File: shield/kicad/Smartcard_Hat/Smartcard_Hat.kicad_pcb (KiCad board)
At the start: 2 copper layers, 68.6 x 53.3 mm, 11 parts, among them J1 7712P0225A25LF, U6 ST8034HNQR

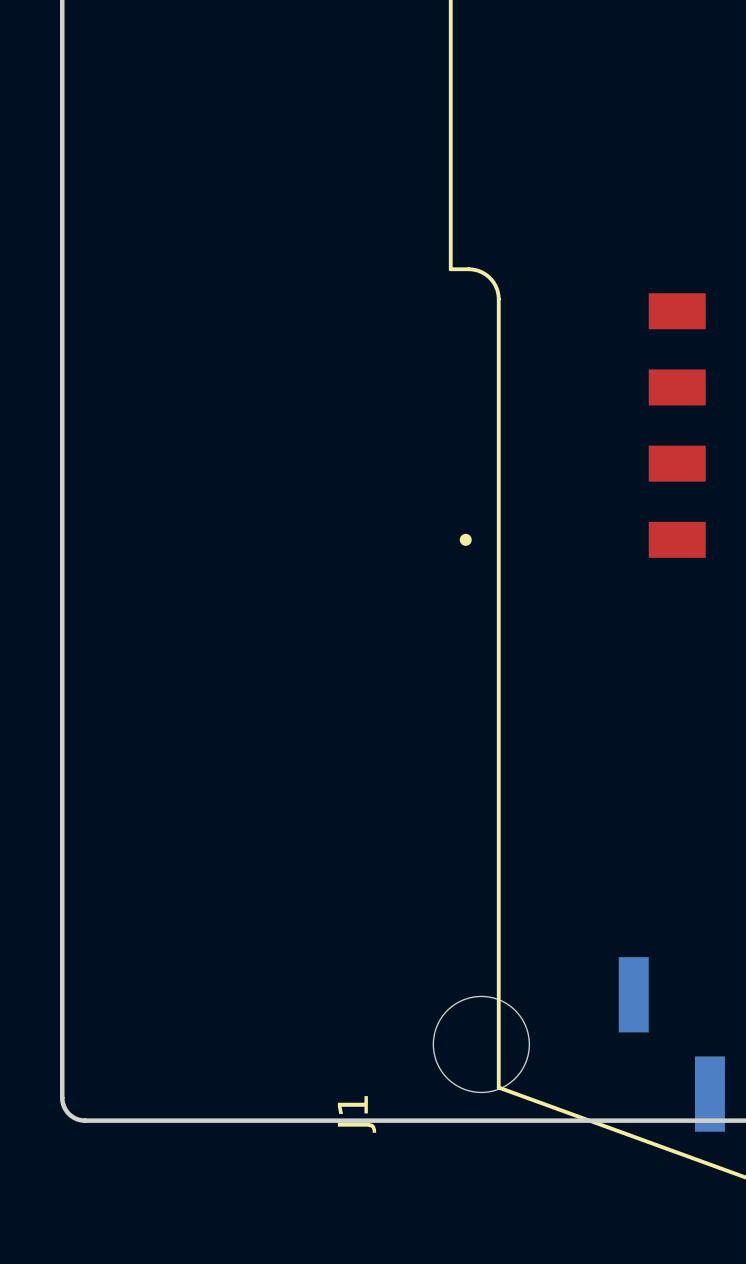
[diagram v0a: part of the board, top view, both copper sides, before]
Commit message: add basic qr scanner
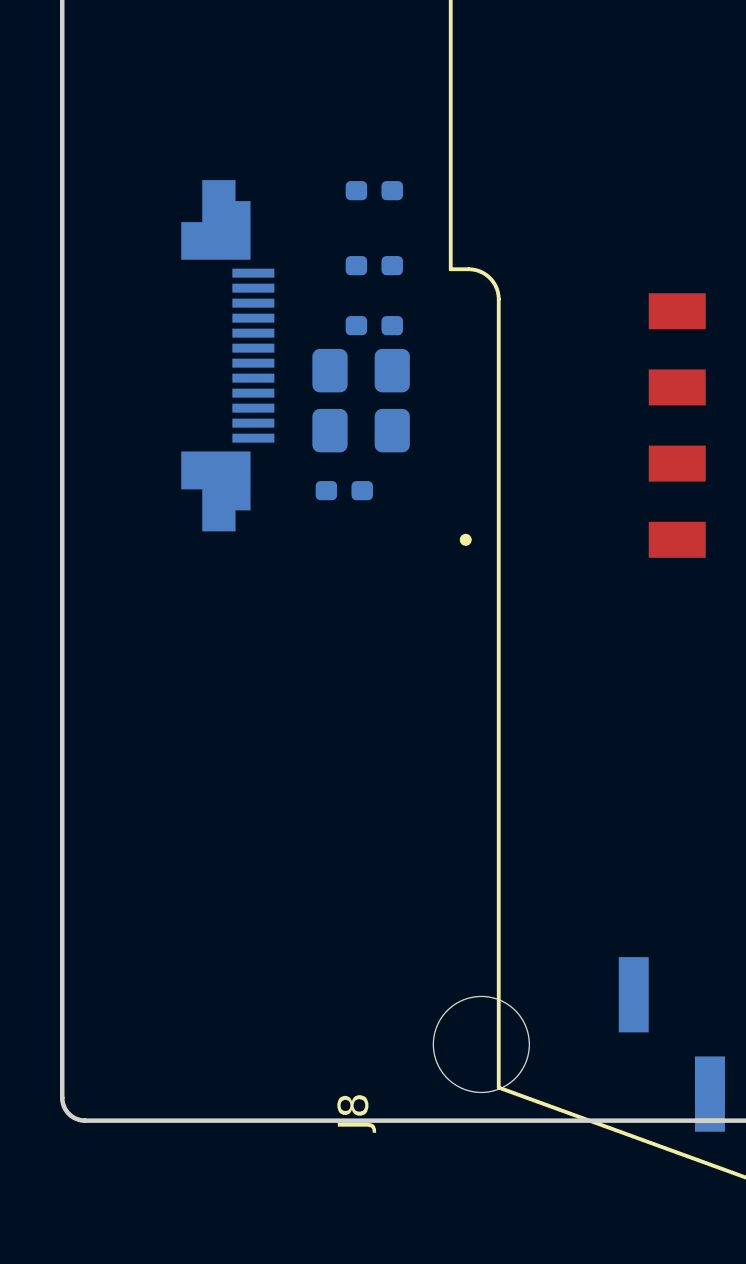
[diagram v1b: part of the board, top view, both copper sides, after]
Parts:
- added C41: 1u, Capacitor_SMD:C_0805_2012Metric_Pad1.18x1.45mm_HandSolder, B.Cu at (110.0, 75.0)
- added C42: 22u, Capacitor_SMD:C_0805_2012Metric_Pad1.18x1.45mm_HandSolder, B.Cu at (110.0, 77.0)
- added J10: SFV12R-2STE1HLF, Library:AMPHENOL_SFV12R-2STE1HLF, B.Cu at (104.0, 74.5)
- added R48: 10k, Resistor_SMD:R_0402_1005Metric_Pad0.72x0.64mm_HandSolder, B.Cu at (110.4, 69.0)
- added R49: 10k, Resistor_SMD:R_0402_1005Metric_Pad0.72x0.64mm_HandSolder, B.Cu at (110.4, 71.5)
- added R50: 10k, Resistor_SMD:R_0402_1005Metric_Pad0.72x0.64mm_HandSolder, B.Cu at (109.4, 79.0)
- added R51: 200R, Resistor_SMD:R_0402_1005Metric_Pad0.72x0.64mm_HandSolder, B.Cu at (110.4, 73.5)
- renumbered J1 to J8
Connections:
- J12 pad 1: /7 -> /QR_UART_TX
- J12 pad 2: /*6 -> /QR_UART_RX
- J12 pad 3: /*5 -> unconnected-(J12-Pin_3-Pad3)
- J12 pad 4: /4 -> unconnected-(J12-Pin_4-Pad4)
- J12 pad 5: /*3 -> unconnected-(J12-Pin_5-Pad5)
- J12 pad 6: /2 -> unconnected-(J12-Pin_6-Pad6)
- J12 pad 7: /TX/1 -> unconnected-(J12-Pin_7-Pad7)
- J12 pad 8: /RX/0 -> unconnected-(J12-Pin_8-Pad8)
- J8 pad C1: Net-(J1-VCC) -> Net-(J8-VCC)
- J8 pad C2: Net-(J1-RST) -> Net-(J8-RST)
- J8 pad C3: Net-(J1-CLK) -> Net-(J8-CLK)
- J8 pad C4: Net-(J1-RFU) -> Net-(J8-RFU)
- J8 pad C7: Net-(J1-I/O) -> Net-(J8-I/O)
- J8 pad C8: Net-(J1-RFU__1) -> Net-(J8-RFU__1)

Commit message: re-org
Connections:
- net /NRST renamed /STM32F469I-DISCO-Interface/NRST
- net /QR_BEEP renamed /QR_Scanner/QR_BEEP
- J10 pad 10: /QR_TRIG -> unconnected-(J10-Pad10)
- J10 pad 12: unconnected-(J10-Pad12) -> /QR_Scanner/QR_TRIG
- J10 pad 5: /QR_UART_TX -> /QR_Scanner/QR_UART_TX
- J11 pad 1: /SCL/A5 -> unconnected-(J11-Pin_1-Pad1)
- J11 pad 10: /8 -> unconnected-(J11-Pin_10-Pad10)
- J11 pad 2: /SDA/A4 -> unconnected-(J11-Pin_2-Pad2)
- J11 pad 3: /AREF -> unconnected-(J11-Pin_3-Pad3)
- J11 pad 5: /13 -> unconnected-(J11-Pin_5-Pad5)
- J11 pad 6: /12 -> unconnected-(J11-Pin_6-Pad6)
- J11 pad 7: /*11 -> unconnected-(J11-Pin_7-Pad7)
- J11 pad 8: /*10 -> unconnected-(J11-Pin_8-Pad8)
- J11 pad 9: /*9 -> unconnected-(J11-Pin_9-Pad9)
- J12 pad 1: /QR_UART_TX -> /STM32F469I-DISCO-Interface/QR_UART_TX
- J12 pad 2: /QR_UART_RX -> /STM32F469I-DISCO-Interface/QR_UART_RX
- J13 pad 1: /A0 -> unconnected-(J13-Pin_1-Pad1)
- J13 pad 2: /A1 -> unconnected-(J13-Pin_2-Pad2)
- J13 pad 3: /A2 -> unconnected-(J13-Pin_3-Pad3)
- J13 pad 4: /A3 -> unconnected-(J13-Pin_4-Pad4)
- J13 pad 5: /SDA/A4 -> unconnected-(J13-Pin_5-Pad5)
- J13 pad 6: /SCL/A5 -> unconnected-(J13-Pin_6-Pad6)
- J8 pad NO: Net-(U6-*PRES) -> Net-(U1-*PRES)
- R48 pad 2: /QR_TRIG -> /QR_Scanner/QR_TRIG
- R49 pad 2: /QR_UART_TX -> /QR_Scanner/QR_UART_TX
- R51 pad 1: /QR_UART_RX -> /QR_Scanner/QR_UART_RX
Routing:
- net (no net): track 0.00 -> 2.35 mm
- net /SDA/A4: track 1.18 -> 0.00 mm
- net /SCL/A5: track 1.18 -> 0.00 mm

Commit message: wip
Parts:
- added C28: u1, Capacitor_SMD:C_0805_2012Metric_Pad1.18x1.45mm_HandSolder, F.Cu at (151.1, 71.0)
- added C29: u1, Capacitor_SMD:C_0805_2012Metric_Pad1.18x1.45mm_HandSolder, F.Cu at (151.1, 74.0)
- added C30: u1, Capacitor_SMD:C_0805_2012Metric_Pad1.18x1.45mm_HandSolder, F.Cu at (151.1, 77.1)
- added C31: u1, Capacitor_SMD:C_0805_2012Metric_Pad1.18x1.45mm_HandSolder, F.Cu at (151.1, 80.1)
- added C32: u1, Capacitor_SMD:C_0805_2012Metric_Pad1.18x1.45mm_HandSolder, F.Cu at (151.1, 83.1)
- added C33: u1, Capacitor_SMD:C_0805_2012Metric_Pad1.18x1.45mm_HandSolder, F.Cu at (155.9, 71.0)
- added C34: u1, Capacitor_SMD:C_0805_2012Metric_Pad1.18x1.45mm_HandSolder, F.Cu at (155.9, 74.0)
- added C35: 22u, Capacitor_SMD:C_0805_2012Metric_Pad1.18x1.45mm_HandSolder, F.Cu at (155.9, 77.1)
- added C36: u1, Capacitor_SMD:C_0805_2012Metric_Pad1.18x1.45mm_HandSolder, F.Cu at (155.9, 80.1)
- added C39: 1n, Capacitor_SMD:C_0805_2012Metric_Pad1.18x1.45mm_HandSolder, F.Cu at (155.9, 83.1)
- added R31: 24k, Resistor_SMD:R_0402_1005Metric_Pad0.72x0.64mm_HandSolder, F.Cu at (159.9, 70.5)
- added R32: 10k, Resistor_SMD:R_0402_1005Metric_Pad0.72x0.64mm_HandSolder, F.Cu at (159.9, 72.5)
- added R33: 10k, Resistor_SMD:R_0402_1005Metric_Pad0.72x0.64mm_HandSolder, F.Cu at (159.9, 74.5)
- added R34: 10k, Resistor_SMD:R_0402_1005Metric_Pad0.72x0.64mm_HandSolder, F.Cu at (159.9, 76.5)
- added R35: 10k, Resistor_SMD:R_0402_1005Metric_Pad0.72x0.64mm_HandSolder, F.Cu at (159.9, 78.5)
- added R36: 200R, Resistor_SMD:R_0402_1005Metric_Pad0.72x0.64mm_HandSolder, F.Cu at (163.2, 70.5)
- added R40: 200R, Resistor_SMD:R_0402_1005Metric_Pad0.72x0.64mm_HandSolder, F.Cu at (163.2, 72.5)
- added R41: 200R, Resistor_SMD:R_0402_1005Metric_Pad0.72x0.64mm_HandSolder, F.Cu at (163.2, 74.5)
- added R42: 200R, Resistor_SMD:R_0402_1005Metric_Pad0.72x0.64mm_HandSolder, F.Cu at (163.2, 76.5)
- added R43: 10k, Resistor_SMD:R_0402_1005Metric_Pad0.72x0.64mm_HandSolder, F.Cu at (163.2, 78.5)
- added R44: 200R, Resistor_SMD:R_0402_1005Metric_Pad0.72x0.64mm_HandSolder, F.Cu at (166.4, 70.5)
- added R45: 11.3k, Resistor_SMD:R_0402_1005Metric_Pad0.72x0.64mm_HandSolder, F.Cu at (166.4, 72.5)
- added R46: 10k, Resistor_SMD:R_0402_1005Metric_Pad0.72x0.64mm_HandSolder, F.Cu at (166.4, 74.5)
- added R47: 10k, Resistor_SMD:R_0402_1005Metric_Pad0.72x0.64mm_HandSolder, F.Cu at (166.4, 76.5)
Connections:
- J11 pad 1: unconnected-(J11-Pin_1-Pad1) -> /STM32F469I-DISCO-Interface/SC_RST
- J11 pad 2: unconnected-(J11-Pin_2-Pad2) -> /STM32F469I-DISCO-Interface/SC_AUX2
- J11 pad 4: GND -> unconnected-(J11-Pin_4-Pad4)
- J11 pad 7: unconnected-(J11-Pin_7-Pad7) -> GND
- J12 pad 3: unconnected-(J12-Pin_3-Pad3) -> /STM32F469I-DISCO-Interface/QR_TRIG
- J12 pad 4: unconnected-(J12-Pin_4-Pad4) -> /STM32F469I-DISCO-Interface/UC_BEEP
- J12 pad 5: unconnected-(J12-Pin_5-Pad5) -> /STM32F469I-DISCO-Interface/SC_CLKDIV2
- J12 pad 6: unconnected-(J12-Pin_6-Pad6) -> /STM32F469I-DISCO-Interface/SC_IO
- J12 pad 7: unconnected-(J12-Pin_7-Pad7) -> /STM32F469I-DISCO-Interface/SC_AUX1
- J12 pad 8: unconnected-(J12-Pin_8-Pad8) -> /STM32F469I-DISCO-Interface/SC_CLKDIV1
- J13 pad 2: unconnected-(J13-Pin_2-Pad2) -> /STM32F469I-DISCO-Interface/SC_nOFF
- J13 pad 3: unconnected-(J13-Pin_3-Pad3) -> /STM32F469I-DISCO-Interface/SC_VCC_SEL1
- J13 pad 4: unconnected-(J13-Pin_4-Pad4) -> /STM32F469I-DISCO-Interface/SC_VCC_SEL2
- J13 pad 5: unconnected-(J13-Pin_5-Pad5) -> /STM32F469I-DISCO-Interface/SC_nCMDVCC
- J13 pad 6: unconnected-(J13-Pin_6-Pad6) -> /STM32F469I-DISCO-Interface/SC_CLK

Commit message: wip
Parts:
- added R52: 10k, Resistor_SMD:R_0402_1005Metric_Pad0.72x0.64mm_HandSolder, B.Cu at (155.9, 62.0)
- C28, C29, C30, C31, C32, C33, C34, C35, C36, C39, R31, R32, R33, R34, R35, R36, R40, R41, R42, R43, R45, R46, R47: moved to B.Cu
- R44: value 200R -> 22R; moved to B.Cu
- moved R43 35.1 mm to (128.6, 84.5)
- moved R41 31.1 mm to (132.1, 73.0), turned to 180 degrees
- moved R42 26.6 mm to (136.6, 75.0)
- moved U6 20.5 mm to (134.4, 86.8)
- moved R35 20.4 mm to (141.6, 87.5), turned to 180 degrees
- moved R36 12.8 mm to (150.4, 70.5), turned to 180 degrees
- moved R40 12.8 mm to (150.4, 72.5), turned to 180 degrees
- moved C28 11.4 mm to (162.5, 71.0), turned to 180 degrees
- moved C29 11.4 mm to (162.5, 74.0), turned to 180 degrees
- moved C30 11.4 mm to (162.5, 77.1), turned to 180 degrees
- moved C31 11.4 mm to (162.5, 80.1), turned to 180 degrees
- moved C32 11.4 mm to (162.5, 83.1), turned to 180 degrees
- moved R31 6.29 mm to (153.6, 70.5), turned to 180 degrees
- moved R32 6.29 mm to (153.6, 72.5), turned to 180 degrees
- moved R33 6.29 mm to (153.6, 74.5), turned to 180 degrees
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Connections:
- C30 pad 1: GND -> Net-(J8-VCC)
- C30 pad 2: Net-(J8-VCC) -> GND
- C31 pad 1: GND -> Net-(J8-VCC)
- C31 pad 2: Net-(J8-VCC) -> GND
- C39 pad 1: Net-(U1-PORADJ) -> Net-(U6-PORADJ)
- J8 pad NO: Net-(U1-*PRES) -> Net-(U6-*PRES)
- R31 pad 2: Net-(U1-*OFF) -> /SmartCard_Reader/SC_nOFF
- R35 pad 2: /SmartCard_Reader/SC_nCMDVCC -> Net-(U6-*CMDVCC)
- R36 pad 1: Net-(U1-*OFF) -> /SmartCard_Reader/SC_nCMDVCC
- R36 pad 2: /SmartCard_Reader/SC_nOFF -> Net-(U6-*CMDVCC)
- R40 pad 2: Net-(U1-I/OUC) -> Net-(U6-I/OUC)
- R41 pad 2: Net-(U1-AUXUC1) -> Net-(U6-AUXUC1)
- R42 pad 2: Net-(U1-AUXUC2) -> Net-(U6-AUXUC2)
- R43 pad 2: Net-(U1-PORADJ) -> Net-(U6-PORADJ)
- R44 pad 2: Net-(U1-XTAL1) -> Net-(U6-XTAL1)
- R45 pad 1: Net-(U1-PORADJ) -> Net-(U6-PORADJ)
- U6 pad 1: unconnected-(U6-VDD(INTF)-Pad1) -> +3V3
- U6 pad 10: Net-(J1-RFU) -> Net-(J8-RFU)
- U6 pad 11: Net-(J1-RFU__1) -> Net-(J8-RFU__1)
- U6 pad 13: Net-(J1-CLK) -> Net-(J8-CLK)
- U6 pad 14: Net-(J1-RST) -> Net-(J8-RST)
- U6 pad 15: Net-(J1-VCC) -> Net-(J8-VCC)
- U6 pad 18: unconnected-(U6-PORADJ-Pad18) -> Net-(U6-PORADJ)
- U6 pad 19: unconnected-(U6-*OFF-Pad19) -> /SmartCard_Reader/SC_nOFF
- U6 pad 2: unconnected-(U6-VCC_SEL2-Pad2) -> /SmartCard_Reader/SC_VCC_SEL2
- U6 pad 20: unconnected-(U6-I/OUC-Pad20) -> Net-(U6-I/OUC)
- U6 pad 21: unconnected-(U6-AUXUC1-Pad21) -> Net-(U6-AUXUC1)
- U6 pad 22: unconnected-(U6-AUXUC2-Pad22) -> Net-(U6-AUXUC2)
- U6 pad 23: unconnected-(U6-XTAL1-Pad23) -> Net-(U6-XTAL1)
- U6 pad 3: unconnected-(U6-RSTIN-Pad3) -> /SmartCard_Reader/SC_RST
- U6 pad 4: unconnected-(U6-VCC_SEL1-Pad4) -> /SmartCard_Reader/SC_VCC_SEL1
- U6 pad 5: unconnected-(U6-*CMDVCC-Pad5) -> Net-(U6-*CMDVCC)
- U6 pad 6: unconnected-(U6-CLKDIV1-Pad6) -> /SmartCard_Reader/SC_CLKDIV1
- U6 pad 7: unconnected-(U6-CLKDIV2-Pad7) -> /SmartCard_Reader/SC_CLKDIV2
- U6 pad 9: Net-(J1-I/O) -> Net-(J8-I/O)

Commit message: wip
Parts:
- removed MH1, MH2, MH3, MH4: MountingHole_3.2mm, Arduino_MountingHole:MountingHole_3.2mm
- C28, C29, C30, C31, C32, C33, C34, C39, C41, C42, J10, R31, R36, R40, R41, R42, R43, R44, R45, R48, R49, R50, R51, R52: moved to F.Cu
- J11: footprint Connector_PinHeader_2.54mm:PinHeader_1x10_P2.54mm_Vertical_SMD_Pin1Left -> Connector_PinHeader_2.54mm:PinHeader_1x10_P2.54mm_Vertical_SMD_Pin1Right
- J12, J9: footprint Connector_PinHeader_2.54mm:PinHeader_1x08_P2.54mm_Vertical_SMD_Pin1Left -> Connector_PinHeader_2.54mm:PinHeader_1x08_P2.54mm_Vertical_SMD_Pin1Right
- J13: footprint Connector_PinHeader_2.54mm:PinHeader_1x06_P2.54mm_Vertical_SMD_Pin1Left -> Connector_PinHeader_2.54mm:PinHeader_1x06_P2.54mm_Vertical_SMD_Pin1Right
- J8: footprint 7312P0225A13LF:AMPHENOL_7312P0225A13LF -> Library:AMPHENOL_7312P0225A13LF
- U6: footprint footprints:QFN24_4x4x0.8_STM -> Library:QFN24_4x4x0.8_STM; moved to F.Cu
- moved J11 61.7 mm to (177.2, 69.0), turned to 0 degrees
- moved R43 58.1 mm to (178.0, 53.9), turned to 90 degrees
- moved R44 56.8 mm to (128.7, 113.0), turned to 0 degrees
- moved J12 56.4 mm to (177.2, 96.0), turned to 0 degrees
- moved U6 53.4 mm to (167.5, 44.8), turned to -90 degrees
- moved R41 53.2 mm to (176.8, 44.1)
- moved C41 53.2 mm to (160.5, 58.2), turned to -90 degrees
- moved R42 51.8 mm to (176.8, 42.5), turned to 180 degrees
- moved C42 51.6 mm to (158.0, 58.2), turned to -90 degrees
- moved J10 49.6 mm to (150.3, 56.9), turned to 180 degrees
- moved R35 49.4 mm to (163.5, 43.2), turned to -90 degrees
- moved R46 41.4 mm to (163.0, 33.2), turned to 90 degrees
- moved R32 41.2 mm to (166.0, 33.2), turned to 90 degrees
- moved R50 39.4 mm to (142.2, 57.2), turned to 0 degrees
- moved R47 38.6 mm to (168.8, 38.0), turned to -90 degrees
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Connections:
- J10 pad 12: /QR_Scanner/QR_TRIG -> QR_TRIG
- J10 pad 5: /QR_Scanner/QR_UART_TX -> QR_UART_TX
- J10 pad 9: /QR_Scanner/QR_BEEP -> UC_BEEP
- J11 pad 1: /STM32F469I-DISCO-Interface/SC_RST -> SC_RST
- J11 pad 2: /STM32F469I-DISCO-Interface/SC_AUX2 -> SC_AUX2
- J12 pad 1: /STM32F469I-DISCO-Interface/QR_UART_TX -> QR_UART_TX
- J12 pad 2: /STM32F469I-DISCO-Interface/QR_UART_RX -> QR_UART_RX
- J12 pad 3: /STM32F469I-DISCO-Interface/QR_TRIG -> QR_TRIG
- J12 pad 4: /STM32F469I-DISCO-Interface/UC_BEEP -> UC_BEEP
- J12 pad 5: /STM32F469I-DISCO-Interface/SC_CLKDIV2 -> SC_CLKDIV2
- J12 pad 6: /STM32F469I-DISCO-Interface/SC_IO -> SC_IO
- J12 pad 7: /STM32F469I-DISCO-Interface/SC_AUX1 -> SC_AUX1
- J12 pad 8: /STM32F469I-DISCO-Interface/SC_CLKDIV1 -> SC_CLKDIV1
- J13 pad 2: /STM32F469I-DISCO-Interface/SC_nOFF -> SC_nOFF
- J13 pad 3: /STM32F469I-DISCO-Interface/SC_VCC_SEL1 -> SC_VCC_SEL1
- J13 pad 4: /STM32F469I-DISCO-Interface/SC_VCC_SEL2 -> SC_VCC_SEL2
- J13 pad 5: /STM32F469I-DISCO-Interface/SC_nCMDVCC -> SC_nCMDVCC
- J13 pad 6: /STM32F469I-DISCO-Interface/SC_CLK -> SC_CLK
- R31 pad 2: /SmartCard_Reader/SC_nOFF -> Net-(U6-*OFF)
- R32 pad 2: /SmartCard_Reader/SC_CLKDIV1 -> SC_CLKDIV1
- R33 pad 2: /SmartCard_Reader/SC_VCC_SEL2 -> SC_VCC_SEL2
- R34 pad 2: /SmartCard_Reader/SC_VCC_SEL1 -> SC_VCC_SEL1
- R35 pad 2: Net-(U6-*CMDVCC) -> SC_nCMDVCC
- R36 pad 1: /SmartCard_Reader/SC_nCMDVCC -> SC_nOFF
- R36 pad 2: Net-(U6-*CMDVCC) -> Net-(U6-*OFF)
- R40 pad 1: /SmartCard_Reader/SC_IO -> SC_IO
- R41 pad 1: /SmartCard_Reader/SC_AUX1 -> SC_AUX1
- R42 pad 1: /SmartCard_Reader/SC_AUX2 -> SC_AUX2
- R44 pad 1: /SmartCard_Reader/SC_CLK -> SC_CLK
- R46 pad 1: /SmartCard_Reader/SC_CLKDIV2 -> SC_CLKDIV2
- R47 pad 1: /SmartCard_Reader/SC_RST -> SC_RST
- R48 pad 2: /QR_Scanner/QR_TRIG -> QR_TRIG
- R49 pad 2: /QR_Scanner/QR_UART_TX -> QR_UART_TX
- R51 pad 1: /QR_Scanner/QR_UART_RX -> QR_UART_RX
- U6 pad 19: /SmartCard_Reader/SC_nOFF -> Net-(U6-*OFF)
- U6 pad 2: /SmartCard_Reader/SC_VCC_SEL2 -> SC_VCC_SEL2
- U6 pad 3: /SmartCard_Reader/SC_RST -> SC_RST
- U6 pad 4: /SmartCard_Reader/SC_VCC_SEL1 -> SC_VCC_SEL1
- U6 pad 5: Net-(U6-*CMDVCC) -> SC_nCMDVCC
- U6 pad 6: /SmartCard_Reader/SC_CLKDIV1 -> SC_CLKDIV1
- U6 pad 7: /SmartCard_Reader/SC_CLKDIV2 -> SC_CLKDIV2
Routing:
- net +3V3: track 0.00 -> 71.4 mm, vias 0 -> 1
- net GND: track 1.18 -> 31.2 mm, vias 0 -> 1
- net Net-(J10-Pad4): track 0.00 -> 13.0 mm
- net QR_UART_TX: track 0.00 -> 11.6 mm
- net Net-(U6-*OFF): track 0.00 -> 9.15 mm
- net Net-(U6-XTAL1): track 0.00 -> 8.15 mm
- net Net-(U6-AUXUC2): track 0.00 -> 7.66 mm
- net Net-(U6-AUXUC1): track 0.00 -> 7.16 mm
- net Net-(U6-I/OUC): track 0.00 -> 6.95 mm
- net QR_TRIG: track 0.00 -> 4.89 mm
- net (no net): track 2.35 -> 0.00 mm
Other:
- board size 68.6 x 53.3 mm -> 60 x 127 mm

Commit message: wip
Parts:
- added R1000: 0R, Resistor_SMD:R_0805_2012Metric_Pad1.20x1.40mm_HandSolder, F.Cu at (161.2, 46.8)
- added R1001: 0R, Resistor_SMD:R_0805_2012Metric_Pad1.20x1.40mm_HandSolder, F.Cu at (167.5, 38.0)
- C35, C36: moved to F.Cu
- J8: footprint Library:AMPHENOL_7312P0225A13LF -> 7312P0225A13LF:AMPHENOL_7312P0225A13LF
- R31, R36, R40, R41, R42, R43, R45, R48, R49, R50, R51, R52: footprint Resistor_SMD:R_0402_1005Metric_Pad0.72x0.64mm_HandSolder -> Resistor_SMD:R_0805_2012Metric_Pad1.20x1.40mm_HandSolder
- R32, R33, R34, R35, R46, R47: footprint Resistor_SMD:R_0402_1005Metric_Pad0.72x0.64mm_HandSolder -> Resistor_SMD:R_0805_2012Metric_Pad1.20x1.40mm_HandSolder; moved to F.Cu
- R44: footprint Resistor_SMD:R_0402_1005Metric_Pad0.72x0.64mm_HandSolder -> Resistor_SMD:R_0805_2012Metric_Pad1.20x1.40mm_HandSolder; moved to B.Cu
- moved R46 9.51 mm to (162.5, 42.8), turned to 180 degrees
- moved R32 8.96 mm to (158.4, 38.0), turned to -90 degrees
- moved R33 8.36 mm to (165.2, 38.0)
- moved R35 5.96 mm to (160.7, 38.0)
- moved R34 5.51 mm to (163.0, 38.0)
- moved R50 5.37 mm to (137.5, 59.8)
- moved R51 4.98 mm to (137.5, 57.5)
- moved R47 4.19 mm to (167.5, 34.0), turned to 90 degrees
- moved R31 2.94 mm to (174.0, 50.0), turned to 0 degrees
- moved C35 2.86 mm to (170.2, 40.0), turned to 90 degrees
- moved C36 2.02 mm to (167.5, 50.5), turned to 180 degrees
- moved R52 1.50 mm to (176.8, 39.2)
- moved C33 1.25 mm to (172.2, 40.0)
- moved R49 1.25 mm to (141.5, 57.5)
- moved R43 1.08 mm to (179.0, 53.5)
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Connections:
- U6 pad 10: Net-(J8-RFU) -> Net-(U6-AUX1)
- U6 pad 3: SC_RST -> Net-(U6-RSTIN)
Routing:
- net SC_CLKDIV2: track 0.00 -> 141.1 mm, vias 0 -> 1
- net SC_CLKDIV1: track 0.00 -> 134.9 mm, vias 0 -> 1
- net SC_VCC_SEL2: track 0.00 -> 121.9 mm, vias 0 -> 1
- net Net-(U6-*PRES): track 0.00 -> 118.7 mm
- net SC_VCC_SEL1: track 0.00 -> 116.8 mm, vias 0 -> 1
- net +5V: track 0.00 -> 111.5 mm, vias 0 -> 1
- net SC_nCMDVCC: track 0.00 -> 109.6 mm, vias 0 -> 1
- net SC_nOFF: track 0.00 -> 105.1 mm, vias 0 -> 1
- net Net-(U6-XTAL1): track 8.15 -> 111.7 mm, vias 0 -> 1
- net Net-(J8-I/O): track 0.00 -> 83.5 mm
- net Net-(J8-RFU__1): track 0.00 -> 82.3 mm
- net QR_UART_TX: track 11.6 -> 93.7 mm, vias 0 -> 1
- net QR_TRIG: track 4.89 -> 86.6 mm, vias 0 -> 1
- net QR_UART_RX: track 0.00 -> 78.0 mm, vias 0 -> 1
- net SC_RST: track 0.00 -> 68.9 mm, vias 0 -> 1
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- added copper zone on B.Cu, net GND

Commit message: wip
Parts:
- removed R1000, R1001: 0R, Resistor_SMD:R_0805_2012Metric_Pad1.20x1.40mm_HandSolder
- moved C29 2.41 mm to (167.5, 54.5)
- moved C28 2.26 mm to (167.5, 52.5)
- moved C34 1.75 mm to (170.5, 53.5)
- moved C36 1.31 mm to (168.8, 50.0)
- moved C32 1.06 mm to (172.5, 53.5)
- moved C41 1.00 mm to (159.5, 58.2)
- moved C42 0.50 mm to (157.5, 58.2)
- moved C39 0.43 mm to (174.6, 53.5)
- moved R45 0.43 mm to (176.8, 53.5)
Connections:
- U6 pad 10: Net-(U6-AUX1) -> Net-(J8-RFU)
- U6 pad 3: Net-(U6-RSTIN) -> SC_RST
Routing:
- net Net-(U6-*PRES): track 118.7 -> 44.2 mm, vias 0 -> 2
- net Net-(J8-RFU): track 60.3 -> 30.7 mm, vias 0 -> 2
- net Net-(J8-CLK): track 59.6 -> 34.4 mm
- net GND: track 65.3 -> 48.1 mm, vias 7 -> 43
- net Net-(J8-RFU__1): track 82.3 -> 67.9 mm
- net Net-(J8-I/O): track 83.5 -> 69.9 mm
- net +5V: track 111.5 -> 100.8 mm
- net Net-(U6-AUX1): track 4.62 -> 0.00 mm
- net +3V3: track 124.2 -> 119.7 mm
- net Net-(U6-RSTIN): track 3.91 -> 0.00 mm
- net SC_RST: track 68.9 -> 72.3 mm, vias 1 -> 3
- net QR_TRIG: track 86.6 -> 89.6 mm
- net Net-(J8-RST): track 41.9 -> 38.9 mm
- net UC_BEEP: track 58.0 -> 59.7 mm
- net SC_nOFF: track 105.1 -> 106.6 mm
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- added copper zone on F.Cu, net GND
